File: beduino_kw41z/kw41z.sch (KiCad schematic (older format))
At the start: 26 parts

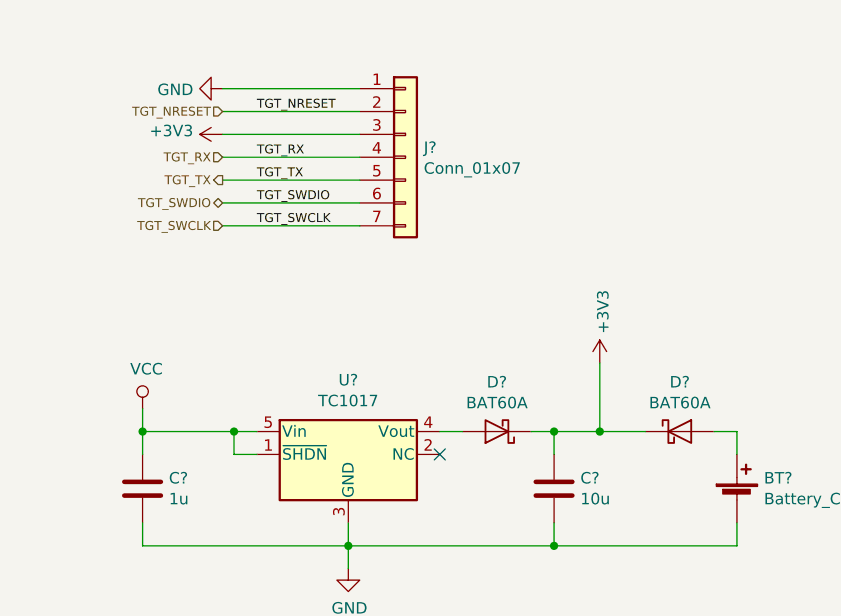
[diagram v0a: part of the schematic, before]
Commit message: Add jumper into the power trace.
This makes it possible to measure the current used by the module.
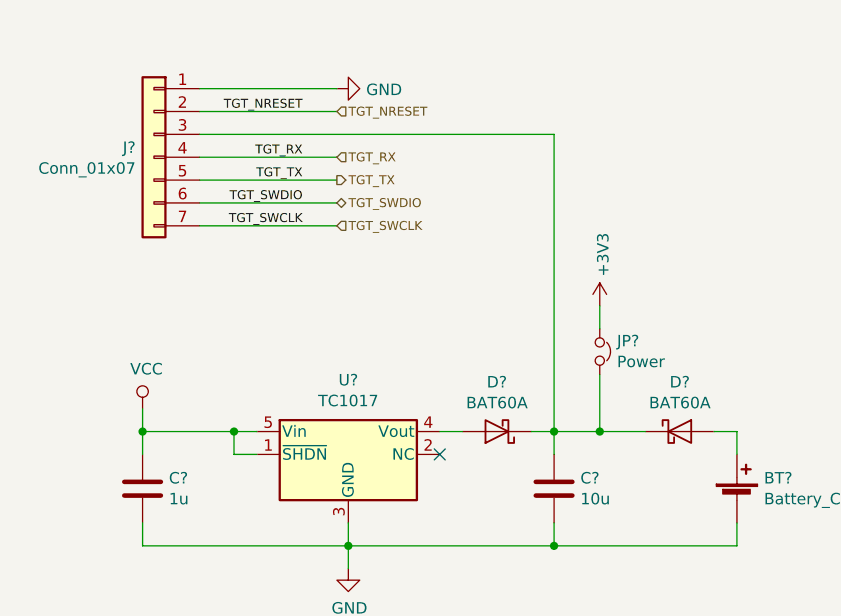
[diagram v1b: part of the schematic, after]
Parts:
- added JP?: Power, symbol Jumper_NC_Small
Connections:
- net +3V3: now also JP?.1; no longer C?.1, D?.1 (K), D?.1 (K), J?.3 (Pin_3)
- new net: C?.1, D?.1 (K), D?.1 (K), J?.3 (Pin_3), JP?.2
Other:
- moved on the sheet: J?
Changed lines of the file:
@@
 Comment4 ""
 $EndDescr
-Text HLabel 1550 1300 0    39   Input ~ 0
+Text HLabel 2050 1300 2    39   Input ~ 0
 TGT_NRESET
-Text HLabel 1550 1700 0    39   BiDi ~ 0
+Text HLabel 2050 1700 2    39   BiDi ~ 0
 TGT_SWDIO
-Text HLabel 1550 1800 0    39   Input ~ 0
+Text HLabel 2050 1800 2    39   Input ~ 0
 TGT_SWCLK
-Text HLabel 1550 1500 0    39   Input ~ 0
+Text HLabel 2050 1500 2    39   Input ~ 0
 TGT_RX
-Text HLabel 1550 1600 0    39   Output ~ 0
+Text HLabel 2050 1600 2    39   Output ~ 0
 TGT_TX
 $Comp
 L Conn_01x07 J?
 U 1 1 5A2111DE
-P 2350 1500
-F 0 "J?" H 2430 1542 50  0000 L CNN
-F 1 "Conn_01x07" H 2430 1451 50  0000 L CNN
-F 2 "" H 2350 1500 50  0001 C CNN
-F 3 "" H 2350 1500 50  0001 C CNN
-	1    2350 1500
-	1    0    0    -1
+P 1250 1500
+F 0 "J?" H 1330 1542 50  0000 L CNN
+F 1 "Conn_01x07" H 1330 1451 50  0000 L CNN
+F 2 "" H 1250 1500 50  0001 C CNN
+F 3 "" H 1250 1500 50  0001 C CNN
+	1    1250 1500
+	-1   0    0    -1
 $EndComp
 $Comp
 L GND #PWR?
 U 1 1 5A2114C3
-P 1550 1200
-F 0 "#PWR?" H 1550 950 50  0001 C CNN
-F 1 "GND" V 1555 1072 50  0000 R CNN
-F 2 "" H 1550 1200 50  0001 C CNN
-F 3 "" H 1550 1200 50  0001 C CNN
-	1    1550 1200
-	0    1    1    0
-$EndComp
-$Comp
-L +3V3 #PWR?
-U 1 1 5A211513
-P 1550 1400
-F 0 "#PWR?" H 1550 1250 50  0001 C CNN
-F 1 "+3V3" V 1565 1528 50  0000 L CNN
-F 2 "" H 1550 1400 50  0001 C CNN
-F 3 "" H 1550 1400 50  0001 C CNN
-	1    1550 1400
-	0    -1   -1   0
-$EndComp
-Wire Wire Line
-	1550 1200 2150 1200
-Wire Wire Line
-	2150 1300 1550 1300
-Wire Wire Line
-	1550 1400 2150 1400
-Wire Wire Line
-	2150 1500 1550 1500
-Wire Wire Line
-	1550 1600 2150 1600
-Wire Wire Line
-	2150 1700 1550 1700
-Wire Wire Line
-	1550 1800 2150 1800
-Text Label 1700 1300 0    39   ~ 0
+P 2050 1200
+F 0 "#PWR?" H 2050 950 50  0001 C CNN
+F 1 "GND" V 2055 1072 50  0000 R CNN
+F 2 "" H 2050 1200 50  0001 C CNN
+F 3 "" H 2050 1200 50  0001 C CNN
+	1    2050 1200
+	0    -1   1    0
+$EndComp
+Wire Wire Line
+	2050 1200 1450 1200
+Wire Wire Line
+	1450 1300 2050 1300
+Wire Wire Line
+	1450 1400 3000 1400
+Wire Wire Line
+	1450 1500 2050 1500
+Wire Wire Line
+	2050 1600 1450 1600
+Wire Wire Line
+	1450 1700 2050 1700
+Wire Wire Line
+	2050 1800 1450 1800
+Text Label 1900 1300 2    39   ~ 0
 TGT_NRESET
-Text Label 1700 1500 0    39   ~ 0
+Text Label 1900 1500 2    39   ~ 0
 TGT_RX
-Text Label 1700 1600 0    39   ~ 0
+Text Label 1900 1600 2    39   ~ 0
 TGT_TX
-Text Label 1700 1700 0    39   ~ 0
+Text Label 1900 1700 2    39   ~ 0
 TGT_SWDIO
-Text Label 1700 1800 0    39   ~ 0
+Text Label 1900 1800 2    39   ~ 0
 TGT_SWCLK
 $Comp
@@
 L +3V3 #PWR?
 U 1 1 5A22B297
-P 3200 2400
-F 0 "#PWR?" H 3200 2250 50  0001 C CNN
-F 1 "+3V3" V 3215 2528 50  0000 L CNN
-F 2 "" H 3200 2400 50  0001 C CNN
-F 3 "" H 3200 2400 50  0001 C CNN
-	1    3200 2400
+P 3200 2150
+F 0 "#PWR?" H 3200 2000 50  0001 C CNN
+F 1 "+3V3" V 3215 2278 50  0000 L CNN
+F 2 "" H 3200 2150 50  0001 C CNN
+F 3 "" H 3200 2150 50  0001 C CNN
+	1    3200 2150
 	1    0    0    -1
 $EndComp
@@
 	2500 2700 2600 2700
 Wire Wire Line
-	3000 2700 3000 2800
+	3000 1400 3000 2800
 Wire Wire Line
 	3000 3200 3000 3100
@@
 	3800 2800 3800 2700
 Connection ~ 3000 2700
-Wire Wire Line
-	3200 2700 3200 2400
 $Comp
 L D_Schottky D?
@@
 Text Notes 5150 4550 0    59   ~ 0
 10pf loading capacitance\nintegrated into the MCU
+$Comp
+L Jumper_NC_Small JP?
+U 1 1 5A2547D3
+P 3200 2350
+F 0 "JP?" V 3154 2425 50  0000 L CNN
+F 1 "Power" V 3245 2425 50  0000 L CNN
+F 2 "" H 3200 2350 50  0001 C CNN
+F 3 "" H 3200 2350 50  0001 C CNN
+	1    3200 2350
+	0    1    1    0
+$EndComp
+Wire Wire Line
+	3200 2700 3200 2450
+Wire Wire Line
+	3200 2250 3200 2150
 $EndSCHEMATC

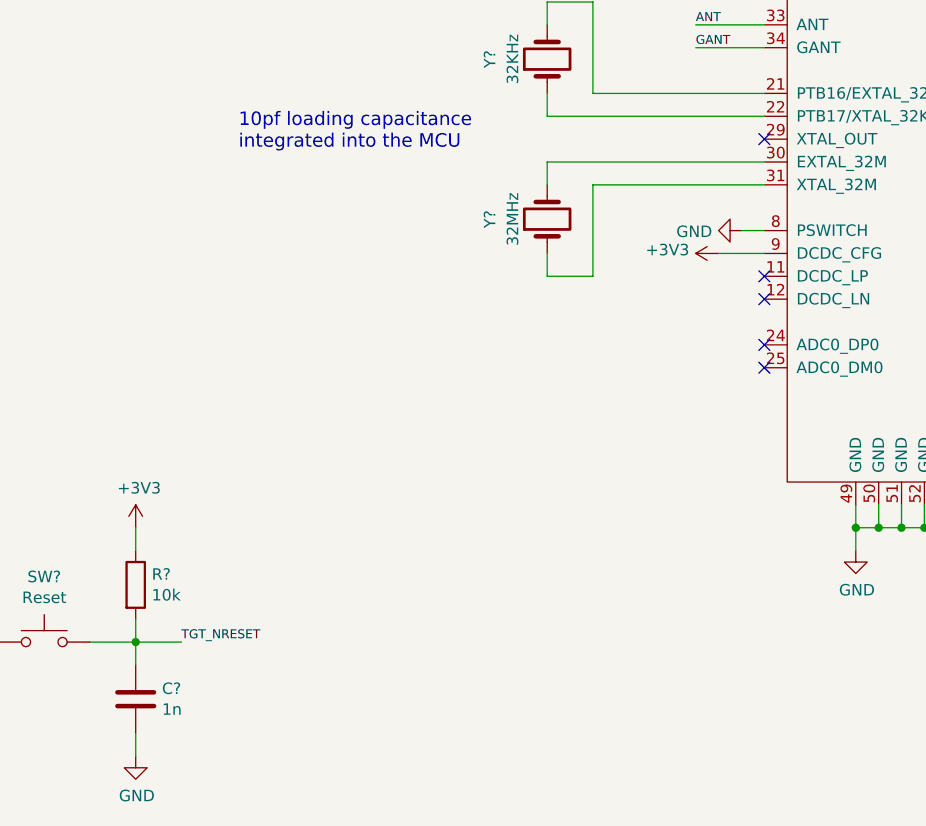
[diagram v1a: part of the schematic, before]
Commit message: Change 32MHz Crystal to a 4 pin type.
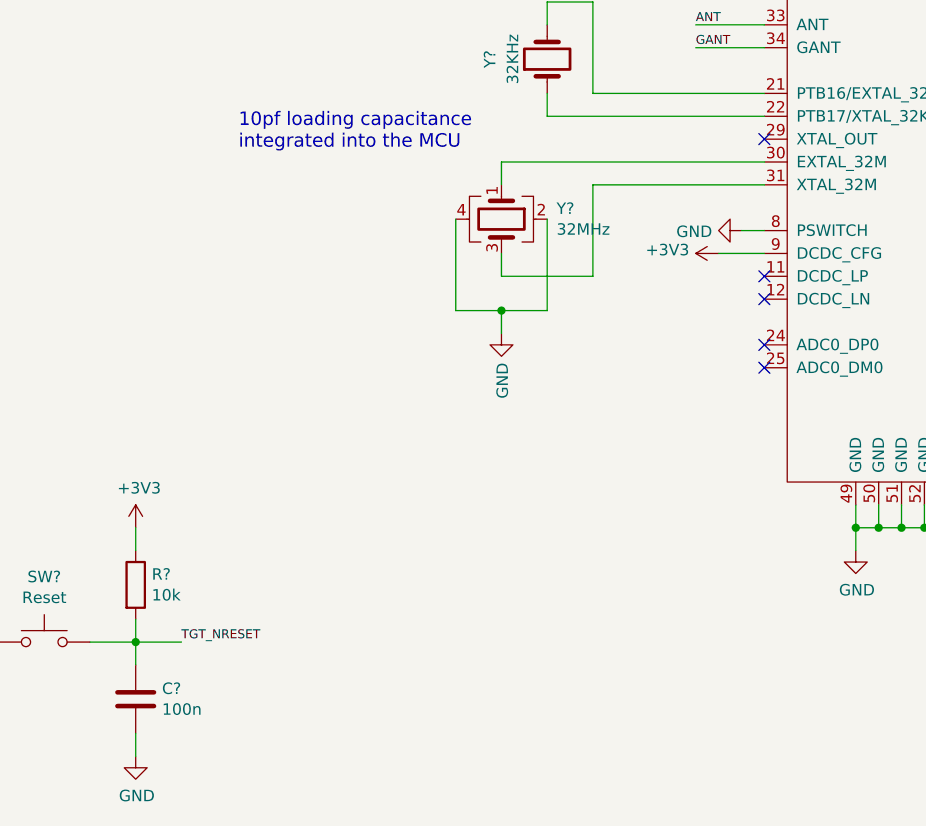
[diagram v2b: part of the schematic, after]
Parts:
- removed Y?: 32MHz, symbol Crystal
- added Y?: 32MHz, Crystals:Crystal_SMD_3225-4pin_3.2x2.5mm, symbol Crystal_GND24
- C?: value 1n -> 100n
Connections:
- net GND: now also Y?.2, Y?.4
- net at U?.30 (EXTAL_32M): now also Y?.1
- net at U?.31 (XTAL_32M): now also Y?.3
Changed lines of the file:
@@
 	7900 1550 7900 1650
 Wire Wire Line
-	6500 4700 6500 4600
-Wire Wire Line
-	6500 4600 7450 4600
+	6300 4600 7450 4600
 Wire Wire Line
 	6500 4300 6500 4400
@@
 	6700 4300 7450 4300
 Wire Wire Line
-	6500 5000 6500 5100
-Wire Wire Line
-	6500 5100 6700 5100
+	6300 5100 6700 5100
 Wire Wire Line
 	6700 5100 6700 4700
 Wire Wire Line
 	6700 4700 7450 4700
-$Comp
-L Crystal Y?
-U 1 1 5A23195A
-P 6500 4850
-F 0 "Y?" H 6500 5100 50  0000 C CNN
-F 1 "32MHz" H 6500 5000 50  0000 C CNN
-F 2 "" H 6500 4850 50  0001 C CNN
-F 3 "" H 6500 4850 50  0001 C CNN
-	1    6500 4850
-	0    -1   -1   0
-$EndComp
 Text Label 6900 3500 0    39   ~ 0
 TGT_NRESET
@@
 P 4700 6950
 F 0 "C?" H 4815 6996 50  0000 L CNN
-F 1 "1n" H 4815 6905 50  0000 L CNN
+F 1 "100n" H 4815 6905 50  0000 L CNN
 F 2 "" H 4738 6800 50  0001 C CNN
 F 3 "" H 4700 6950 50  0001 C CNN
@@
 Wire Wire Line
 	3200 2250 3200 2150
+$Comp
+L Crystal_GND24 Y?
+U 1 1 5A256482
+P 6300 4850
+F 0 "Y?" V 6254 5091 50  0000 L CNN
+F 1 "32MHz" V 6345 5091 50  0000 L CNN
+F 2 "Crystals:Crystal_SMD_3225-4pin_3.2x2.5mm" H 6300 4850 50  0001 C CNN
+F 3 "" H 6300 4850 50  0001 C CNN
+	1    6300 4850
+	0    1    1    0
+$EndComp
+Wire Wire Line
+	6300 5100 6300 5000
+Wire Wire Line
+	6300 4700 6300 4600
+Wire Wire Line
+	6500 4850 6500 5250
+Wire Wire Line
+	6500 5250 6100 5250
+Wire Wire Line
+	6100 5250 6100 4850
+$Comp
+L GND #PWR?
+U 1 1 5A256A71
+P 6300 5350
+F 0 "#PWR?" H 6300 5100 50  0001 C CNN
+F 1 "GND" V 6305 5222 50  0000 R CNN
+F 2 "" H 6300 5350 50  0001 C CNN
+F 3 "" H 6300 5350 50  0001 C CNN
+	1    6300 5350
+	1    0    0    -1
+$EndComp
+Wire Wire Line
+	6300 5250 6300 5350
+Connection ~ 6300 5250
 $EndSCHEMATC

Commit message: Update schematic for new KiCAD version.
Also add some components.
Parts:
- removed AE?: Antenna_Dipole, symbol Antenna_Dipole
- added ANT1: SWRA117D, MyAntennas:SWRA117D, symbol MyAntennas:SWRA117D
- BT1: renamed from BT?; footprint (none) -> Battery_Holders:Keystone_1058_1x2032-CoinCell; symbol Battery_Cell -> device:Battery_Cell
- C10, C11, C13, C14, C15, C16, C17: renamed from C?; footprint (none) -> Capacitors_SMD:C_0603_HandSoldering; symbol C -> device:C
- C12, C9: renamed from C?; footprint (none) -> Capacitors_SMD:C_0805_HandSoldering; symbol C -> device:C
- D5, D6: renamed from D?; footprint (none) -> LEDs:LED_0603_HandSoldering; symbol LED -> device:LED
- D7, D8: renamed from D?; footprint (none) -> Diodes_SMD:D_SOD-323; symbol D_Schottky -> device:D_Schottky
- J3: renamed from J?; footprint (none) -> Pin_Headers:Pin_Header_Straight_1x07_Pitch2.54mm; symbol Conn_01x07 -> Connector:Conn_01x07
- JP1: renamed from JP?; footprint (none) -> Pin_Headers:Pin_Header_Straight_1x02_Pitch2.54mm; symbol Jumper_NC_Small -> device:Jumper_NC_Small
- L1: renamed from L?; footprint (none) -> Inductors_SMD:L_0603_HandSoldering; symbol L -> device:L
- R14, R15, R16: renamed from R?; footprint (none) -> Resistors_SMD:R_0603_HandSoldering; symbol R -> device:R
- SW2: renamed from SW?; footprint (none) -> Buttons_Switches_SMD:SW_SPST_B3S-1100; symbol SW_Push -> Switch:SW_Push
- U3: renamed from U?; footprint TO_SOT_Packages_SMD:SOT-23-5 -> TO_SOT_Packages_SMD:SOT-23-5_HandSoldering; symbol TC1017 -> beduino_regul:TC1017
- U4: renamed from U?; footprint (none) -> Pin_Headers:Pin_Header_Straight_2x12_Pitch2.54mm; symbol Module_CONN -> beduino_conn:Module_CONN
- U5: renamed from U?; footprint (none) -> Housings_DFN_QFN:QFN-48-1EP_7x7mm_Pitch0.5mm; symbol MKW41Z -> beduino_nxp:MKW41Z
- Y2: renamed from Y?; footprint Crystals:Crystal_SMD_3225-4pin_3.2x2.5mm -> Crystals:Crystal_SMD_3225-4pin_3.2x2.5mm_HandSoldering; symbol Crystal_GND24 -> device:Crystal_GND24
- Y3: renamed from Y?; footprint (none) -> Crystals:Crystal_SMD_3215-2pin_3.2x1.5mm; symbol Crystal -> device:Crystal
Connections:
- wire segments 151 -> 198

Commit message: Small changes in the schematics.
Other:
- moved on the sheet: C12, D7
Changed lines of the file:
@@
 L device:C C12
 U 1 1 5A22B051
-P 3000 2950
-F 0 "C12" H 3115 2996 50  0000 L CNN
-F 1 "10u" H 3115 2905 50  0000 L CNN
-F 2 "Capacitors_SMD:C_0805_HandSoldering" H 3038 2800 50  0001 C CNN
-F 3 "" H 3000 2950 50  0001 C CNN
-	1    3000 2950
+P 2650 2950
+F 0 "C12" H 2765 2996 50  0000 L CNN
+F 1 "10u" H 2765 2905 50  0000 L CNN
+F 2 "Capacitors_SMD:C_0805_HandSoldering" H 2688 2800 50  0001 C CNN
+F 3 "" H 2650 2950 50  0001 C CNN
+	1    2650 2950
 	1    0    0    -1
 $EndComp
@@
 L device:D_Schottky D7
 U 1 1 5A2331B9
-P 2750 2700
-F 0 "D7" H 2750 2484 50  0000 C CNN
-F 1 "BAT60A" H 2750 2575 50  0000 C CNN
-F 2 "Diodes_SMD:D_SOD-323" H 2750 2700 50  0001 C CNN
-F 3 "" H 2750 2700 50  0001 C CNN
-	1    2750 2700
+P 2800 2700
+F 0 "D7" H 2800 2484 50  0000 C CNN
+F 1 "BAT60A" H 2800 2575 50  0000 C CNN
+F 2 "Diodes_SMD:D_SOD-323" H 2800 2700 50  0001 C CNN
+F 3 "" H 2800 2700 50  0001 C CNN
+	1    2800 2700
 	-1   0    0    1
 $EndComp
 Wire Wire Line
-	2500 2700 2600 2700
-Wire Wire Line
 	3000 1400 3000 2700
 Wire Wire Line
-	3000 3200 3000 3100
-Connection ~ 3000 3200
-Wire Wire Line
 	3800 3200 3800 3100
 Wire Wire Line
 	3800 2800 3800 2700
-Connection ~ 3000 2700
 $Comp
 L device:D_Schottky D8
@@
 Wire Wire Line
 	1200 3200 2100 3200
-Wire Wire Line
-	2900 2700 3000 2700
 Wire Wire Line
 	7850 6100 7850 6200
@@
 	2100 3200 2100 3300
 Wire Wire Line
-	2100 3200 3000 3200
+	2100 3200 2650 3200
 Wire Wire Line
 	2300 6500 2400 6500
@@
 Wire Wire Line
 	2850 7000 2950 7000
-Wire Wire Line
-	3000 3200 3800 3200
-Wire Wire Line
-	3000 2700 3000 2800
 Wire Wire Line
 	3000 2700 3200 2700
@@
 Wire Wire Line
 	3200 2500 3200 2450
+Wire Wire Line
+	2650 2700 2650 2800
+Wire Wire Line
+	2500 2700 2650 2700
+Wire Wire Line
+	2650 3100 2650 3200
+Connection ~ 2650 3200
+Connection ~ 2650 2700
+Wire Wire Line
+	2950 2700 3000 2700
+Wire Wire Line
+	2650 3200 3800 3200
+Connection ~ 3000 2700
 $EndSCHEMATC

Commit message: Update PCB layout.
The connection between the dipdap and the kw41z-mini is now closed with
a small trace. If the trace is cut, added smd pads simplify the creation
of solder jumpers.
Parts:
- ANT1: symbol MyAntennas:SWRA117D -> beduino_antenna:SWRA117D
- BT1: symbol device:Battery_Cell -> Device:Battery_Cell
- C10, C11, C12, C13, C14, C15, C16, C17, C9: symbol device:C -> Device:C
- D5, D6: symbol device:LED -> Device:LED
- D7, D8: symbol device:D_Schottky -> Device:D_Schottky
- J3: symbol Connector:Conn_01x07 -> Connector_Generic:Conn_01x07
- JP1: symbol device:Jumper_NC_Small -> Device:Jumper_NC_Small
- L1: symbol device:L -> Device:L
- R14, R15, R16: symbol device:R -> Device:R
- U3: footprint TO_SOT_Packages_SMD:SOT-23-5_HandSoldering -> TO_SOT_Packages_SMD:SOT-353_SC-70-5
- Y2: symbol device:Crystal_GND24 -> Device:Crystal_GND24
- Y3: symbol device:Crystal -> Device:Crystal
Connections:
- wire segments 198 -> 197
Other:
- moved on the sheet: D7
